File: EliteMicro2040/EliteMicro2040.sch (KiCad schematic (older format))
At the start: 41 parts, among them J2 SKRKAEE020, J5 Conn_01x03_Male, U1 TLV75533PDBVR, U2 Elite-C, U3 RP2040, U4 W25Q32JVSS, Y1 3225_4P

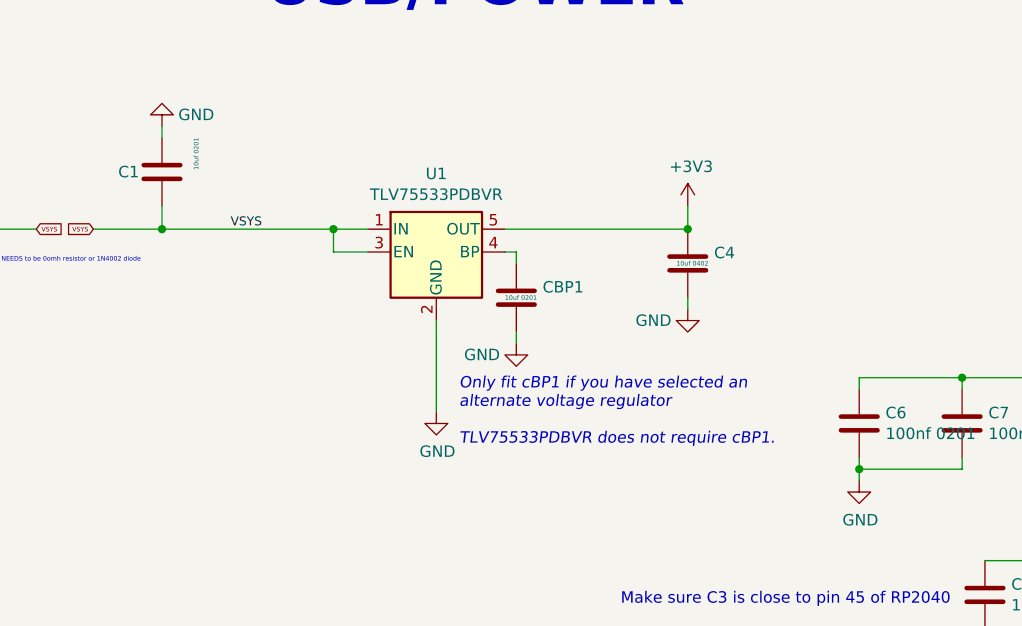
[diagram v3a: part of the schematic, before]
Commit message: Swapped regulator for a smaller one, need to re-arrange some bits it seems.
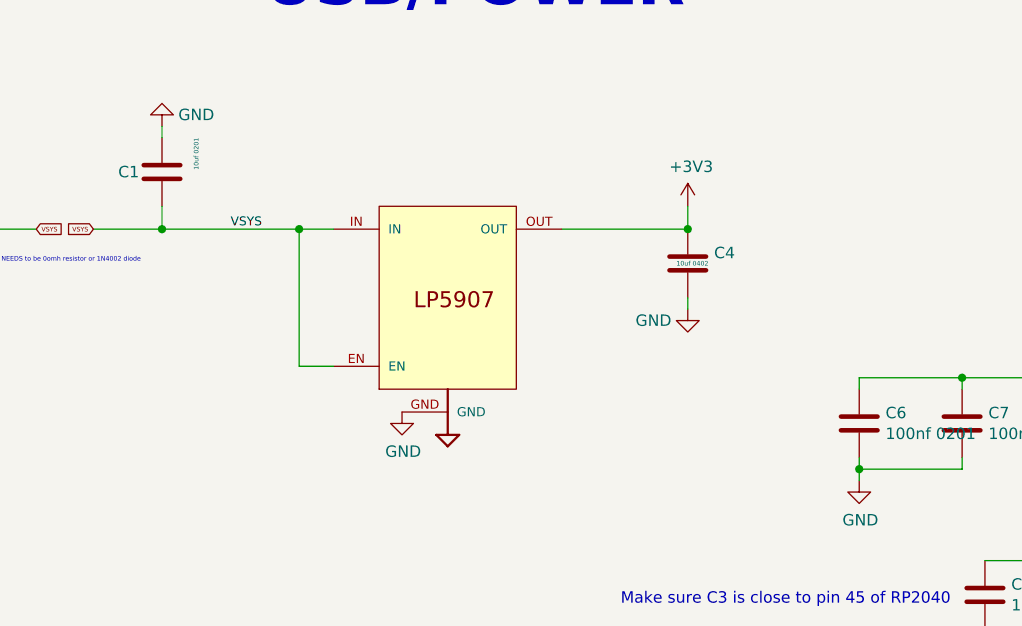
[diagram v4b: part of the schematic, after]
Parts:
- removed CBP1: 10uf 0201, Capacitor_SMD:C_0201_0603Metric, symbol Device:C
- removed U1: TLV75533PDBVR, Package_TO_SOT_SMD:SOT-23-5, symbol Regulator_Linear:AP131-15
- added U1: LP5907UVX-3.3, LP5907UVX-3:DSBGA-4, symbol LP5907UVX-3.3:LP5907UVX-3.3
- J2, RSW1: footprint Jumper:SolderJumper-2_P1.3mm_Bridged_Pad1.0x1.5mm -> Button_Switch_SMD:SW_Push_SPST_NO_Alps_SKRK
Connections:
- net +3V3: now also U1.OUT
- net GND: now also U1.GND
- net VBUS: now also U1.EN, U1.IN
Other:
- note removed: "Only fit cBP1 if you have selected an \nalternate voltage regulator\n\nTLV75533PDBVR does not require cBP1."
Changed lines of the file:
@@
 F 0 "J2" H 1100 5100 50  0000 C CNN
 F 1 "SKRKAEE020" H 1050 4850 50  0000 C CNN
-F 2 "Jumper:SolderJumper-2_P1.3mm_Bridged_Pad1.0x1.5mm" H 1050 4950 50  0001 C CNN
+F 2 "Button_Switch_SMD:SW_Push_SPST_NO_Alps_SKRK" H 1050 4950 50  0001 C CNN
 F 3 "" H 1050 4950 50  0001 C CNN
 F 4 " " H 1050 4950 50  0001 C CNN "LCSC"
@@
 L power:GND #PWR05
 U 1 1 60EAD68C
-P 4350 2550
-F 0 "#PWR05" H 4350 2300 50  0001 C CNN
-F 1 "GND" H 4355 2377 50  0000 C CNN
-F 2 "" H 4350 2550 50  0001 C CNN
-F 3 "" H 4350 2550 50  0001 C CNN
-	1    4350 2550
+P 4200 2550
+F 0 "#PWR05" H 4200 2300 50  0001 C CNN
+F 1 "GND" H 4205 2377 50  0000 C CNN
+F 2 "" H 4200 2550 50  0001 C CNN
+F 3 "" H 4200 2550 50  0001 C CNN
+	1    4200 2550
 	1    0    0    -1
 $EndComp
@@
 $EndComp
 Wire Wire Line
-	3150 1750 3900 1750
-Wire Wire Line
-	4650 1750 5450 1750
-Wire Wire Line
-	4350 2150 4350 2550
-$Comp
-L Device:C CBP1
-U 1 1 6127D24E
-P 4700 2050
-F 0 "CBP1" H 4815 2096 50  0000 L CNN
-F 1 "10uf 0201" H 4650 2050 20  0000 L CNN
-F 2 "Capacitor_SMD:C_0201_0603Metric" H 4738 1900 50  0001 C CNN
-F 3 "" H 4700 2050 50  0001 C CNN
-F 4 " " H 4700 2050 50  0001 C CNN "LCSC"
-	1    4700 2050
-	1    0    0    -1
-$EndComp
-$Comp
-L power:GND #PWR0110
-U 1 1 6127D922
-P 4700 2250
-F 0 "#PWR0110" H 4700 2000 50  0001 C CNN
-F 1 "GND" H 4550 2200 50  0000 C CNN
-F 2 "" H 4700 2250 50  0001 C CNN
-F 3 "" H 4700 2250 50  0001 C CNN
-	1    4700 2250
-	1    0    0    -1
-$EndComp
-Wire Wire Line
-	4700 2250 4700 2200
-Wire Wire Line
-	4700 1900 4700 1850
-Wire Wire Line
-	4700 1850 4650 1850
-Text Notes 4450 2700 0    50   Italic 0
-Only fit cBP1 if you have selected an \nalternate voltage regulator\n\nTLV75533PDBVR does not require cBP1.
+	3150 1750 3750 1750
 Text Notes 2200 6250 0    50   ~ 0
 GD25Q40CEIGR is NOT Compatible\nyou need GD25W16* needs to be a multiple of 8 atleast for circuitpython.
@@
 F 0 "RSW1" H 5700 6300 50  0000 C CNN
 F 1 "SKRKAEE020" H 5750 6400 50  0000 C CNN
-F 2 "Jumper:SolderJumper-2_P1.3mm_Bridged_Pad1.0x1.5mm" H 5700 6500 50  0001 C CNN
+F 2 "Button_Switch_SMD:SW_Push_SPST_NO_Alps_SKRK" H 5700 6500 50  0001 C CNN
 F 3 "~" H 5700 6500 50  0001 C CNN
 	1    5700 6500
@@
 Wire Wire Line
 	13950 5000 14200 5000
-Wire Wire Line
-	3900 1850 3900 1750
-Wire Wire Line
-	3900 1850 4050 1850
-Connection ~ 3900 1750
-Wire Wire Line
-	3900 1750 4050 1750
 $Comp
 L Device:C C5
@@
 Wire Wire Line
 	11400 2400 11750 2400
-$Comp
-L Regulator_Linear:AP131-15 U1
-U 1 1 6128F962
-P 4350 1850
-F 0 "U1" H 4350 2192 50  0000 C CNN
-F 1 "TLV75533PDBVR" H 4350 2101 50  0000 C CNN
-F 2 "Package_TO_SOT_SMD:SOT-23-5" H 4350 2175 50  0001 C CIN
-F 3 "" H 4350 1900 50  0001 C CNN
-F 4 " " H 4350 1850 50  0001 C CNN "LCSC"
-	1    4350 1850
-	1    0    0    -1
-$EndComp
 Wire Wire Line
 	2250 1750 2600 1750
+Wire Wire Line
+	4900 1750 5450 1750
+$Comp
+L LP5907UVX-3.3:LP5907UVX-3.3 U1
+U 1 1 61E09CD5
+P 4400 2050
+F 0 "U1" H 4400 2050 50  0001 L BNN
+F 1 "LP5907UVX-3.3" H 4400 2050 50  0001 L BNN
+F 2 "LP5907UVX-3:DSBGA-4" H 4400 2050 50  0001 L BNN
+F 3 "" H 4400 2050 50  0001 L BNN
+	1    4400 2050
+	1    0    0    -1
+$EndComp
+Wire Wire Line
+	3900 2350 3750 2350
+Wire Wire Line
+	3750 2350 3750 1750
+Connection ~ 3750 1750
+Wire Wire Line
+	3750 1750 3900 1750
 $EndSCHEMATC
